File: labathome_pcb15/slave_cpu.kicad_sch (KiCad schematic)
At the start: 43 parts, among them J1 HALL, J26 STDC14, J27 ADDA, J28 Brushless, J31 Servo1, J32 Servo2, J33 Servo3, SW10 USBPD ADC2 EXT, U3 DRV8313, U5 STM32G431C6Ux, Y1 8MHz/12pF

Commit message: Final PCB as ordered @ JLCPCB
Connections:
- net STM32_RESET: now also J26.12 (Pin_12)
- no-connect marks 8 -> 7
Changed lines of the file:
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@@
-	)
-	(no_connect
-		(at 48.26 113.03)
 	)
 	(no_connect
@@
 			(effects
 				(font
+					(size 1.27 1.27)
+				)
+				(justify left)
+				(hide yes)
+			)
+		)
+	)
+	(global_label "STM32_RESET"
+		(shape output)
+		(at 48.26 113.03 0)
+		(fields_autoplaced yes)
+		(effects
+			(font
+				(size 1.27 1.27)
+			)
+			(justify left)
+		)
+		(property "Intersheetrefs" "${INTERSHEET_REFS}"
+			(at 64.0054 113.03 0)
+			(effects
+				(font

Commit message: lbathome 15.1
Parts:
- removed R65: 10k, Resistor_SMD:R_0402_1005Metric, symbol Device:R
- removed SW10: USBPD ADC2 EXT, liebler_MECH:SW_SPDT_PCM12_handsolder, symbol liebler_MECH:SW_SPDT_with_Case
- removed U5: STM32G431C6Ux, Package_DFN_QFN:QFN-48-1EP_7x7mm_P0.5mm_EP5.6x5.6mm, symbol MCU_ST_STM32G4:STM32G431C6Ux
- removed Y1: 8MHz/12pF, Crystal:Crystal_SMD_3225-4Pin_3.2x2.5mm, symbol Device:Crystal_GND24
- added C52, C63: u1/50V, Capacitor_SMD:C_0603_1608Metric, symbol Device:C
- added C64: u1, Capacitor_SMD:C_0603_1608Metric, symbol Device:C
- added J30: Servo4, liebler_CONN:PinHeader_1x03_P2.54mm_Vertical_smallerCourtyard, symbol Connector_Generic:Conn_01x03
- added J34: STM32 EXT, Connector_PinHeader_2.54mm:PinHeader_2x03_P2.54mm_Vertical, symbol Connector_Generic:Conn_02x03_Odd_Even
- added R38: r1, Resistor_THT:R_Axial_DIN0309_L9.0mm_D3.2mm_P12.70mm_Horizontal, symbol Device:R
- added U16: LM358, Package_SO:SOIC-8_3.9x4.9mm_P1.27mm, symbol Amplifier_Operational:LM358
- added U5: STM32G431R8Tx, Package_QFP:LQFP-64_10x10mm_P0.5mm, symbol MCU_ST_STM32G4:STM32G431R8Tx
- C50: value 15p -> u1
- C61: value 15p -> 4u7/6V3
- FB2: value 600R -> 600R
- J31, J32, J33: footprint Connector_PinHeader_2.54mm:PinHeader_1x03_P2.54mm_Vertical -> liebler_CONN:PinHeader_1x03_P2.54mm_Vertical_smallerCourtyard
- R49: value k22 -> 10k; footprint Resistor_SMD:R_0402_1005Metric -> Resistor_SMD:R_0805_2012Metric_Pad1.20x1.40mm_HandSolder
- R52: value 10k -> 22k; footprint Resistor_SMD:R_0402_1005Metric -> Resistor_SMD:R_0805_2012Metric_Pad1.20x1.40mm_HandSolder; Option (none) -> Sound only
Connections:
- net ADC_IN2_EXT is gone; now on net ADC_IN2: J27.4 (Pin_4)
- net +24V: now also C52.2, C63.1, C64.2, U16.8 (V+)
- net +3V3: now also C50.1, U5.1 (VBAT), U5.16 (VDD), U5.32 (VDD), U5.48 (VDD), U5.64 (VDD); no longer R50.2, R52.2, U3.15 (V3P3)
- net +5V: now also J30.2 (Pin_2)
- net ADC_IN1: now also U5.22 (PC4)
- net ADC_IN2: now also U5.23 (PC5)
- net BL_DRV1: now also U5.38 (PC6)
- net BL_DRV2: now also U5.39 (PC7)
- net BL_DRV3: now also U5.40 (PC8)
- net BL_ENABLEx: now also U5.60 (PB7)
- net BL_FAULT: now also U5.41 (PC9); no longer R50.1
- net BL_HALL1: now also U5.24 (PB0)
- net BL_HALL2: now also U5.21 (PA7)
- net BL_HALL3: now also U5.20 (PA6)
- net BL_RESET: now also U5.55 (PD2)
- net BL_SLEEP: now also U5.42 (PA8); no longer R52.1
- net BRIGHTNESS: now also U5.5 (PF0)
- net BTN_RED: now also U5.61 (PB8)
- net BTN_YEL: now also U5.6 (PF1)
- net DAC1_OUT1: now also U5.18 (PA4)
- net DAC1_OUT2: now also R50.2, U16.3 (+), U5.19 (PA5); no longer J27.2 (Pin_2)
- net FAN2_DRIVE: now also U5.14 (PA2)
- net GND: now also C50.2, C61.2, R49.1, R50.1, C52.1, C63.2, C64.1, J30.3 (Pin_3), R38.2, U16.4 (V-), U5.15 (VSS), U5.27 (VSSA), U5.31 (VSS), U5.47 (VSS), U5.63 (VSS); no longer C50.1, C61.1, U3.10 (PGND3), U3.6 (PGND1), U3.7 (PGND2)
- net HEATER: now also U5.3 (PC14)
- net LED_INFO: now also U5.54 (PC12)
- net LED_WHITE_P: now also U5.17 (PA3)
- net MOVE: now also U5.2 (PC13)
- net ROT_A: now also U5.12 (PA0)
- net ROT_B: now also U5.13 (PA1)
- net Relais: now also U5.4 (PC15)
- net SCL: now also U5.51 (PA15)
- net SDA: now also U5.62 (PB9)
- net STM32_RESET: now also U5.7 (PG10)
- net SWCLK: now also U5.50 (PA14)
- net SWDIO: now also U5.49 (PA13)
- net Servo1: now also U5.8 (PC0)
- net Servo2: now also U5.9 (PC1)
- net Servo3: now also U5.10 (PC2)
- net UART4_RX: now also U5.53 (PC11)
- net UART4_TX: now also U5.52 (PC10)
- net USBPD_CC1: now also U5.43 (PA9), U5.59 (PB6)
- net USBPD_CC2: now also U5.44 (PA10), U5.57 (PB4)
- net USBPD_D+: now also U5.46 (PA12)
- net USBPD_D-: now also U5.45 (PA11)
- net at R49.2: now also R52.2, U16.2 (-); no longer C50.2
- net 24V_SENSE: now reaches R68.2, R69.1
- net 24V_SENSE: now also U5.37 (PB15)
- net at C37.1, C49.1, FB2.1: now also U5.28 (VREF+), U5.29 (VDDA)
- new net: R52.1, U16.1, U16.5 (+)
- new net: C61.1, U3.15 (V3P3)
- new net BL_ISENSE: R38.1, U3.10 (PGND3), U3.6 (PGND1), U3.7 (PGND2), U5.36 (PB14)
- new net DAC1_OUT2x: J27.2 (Pin_2), U16.6 (-), U16.7
- new net OPAMP3+: J34.2 (Pin_2), U5.35 (PB13)
- new net OPAMP3-: J34.3 (Pin_3), U5.26 (PB2)
- new net OPAMP3Q: J34.5 (Pin_5), U5.25 (PB1)
- new net PB12: J34.4 (Pin_4), U5.34 (PB12)
- new net Servo4: J30.1 (Pin_1), U5.11 (PC3)
- new net UART3_RX: J34.1 (Pin_1), U5.33 (PB11)
- new net UART3_TX: J34.6 (Pin_6), U5.30 (PB10)
- no-connect marks 7 -> 5
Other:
- note added: "ADC1.12"
- note added: "BL_DRV=TIM8 Encoder=TIM2 BL_HALL=TIM3 Servos=TIM1 White LED + FAN=TIM15"
- note added: "BOOT0!"
- note added: "I2C1.C"
- note added: "I2C3.C"
- note added: "OPAMP2.+"
- note added: "OPAMP3.+"
- note added: "OPAMP3.-"
- note added: "OPAMP3.OUT"
- note added: "Overcurrent ca. 1,5A"
- note added: "T15.1"
- note added: "T15.2"
- note added: "T17.1N"
- note added: "U2.T"
- note added: "U3.R"
- note added: "U3.T"
- note removed: "ADC1.11"
- note removed: "ADC12.14"
- note removed: "Annahme Streukapaität 5pF Lastkapazität = (12pF-5pF)*2=15pF"
- note removed: "I2C1.D T4.2 T3.4"
- note removed: "Input"
- note removed: "PB13"
- note removed: "PIR?"
- note removed: "Slow Software-PWM!"
- note removed: "T1.1 I2C2.D"
- note removed: "T1.2 I2C2.C T2.3 CC1"
- note removed: "T1.3 T2.4 CC2"
- note removed: "T16.1 T3.1 ADC2.3"
- note removed: "T16.1 T4.3 T8.2 Boot0"
- note removed: "T17.1 T3.2 ADC2.4"
- note removed: "T2.1 ADC12.1"
- note removed: "T2.1 T8.1 I2C1.C"
- note removed: "T2.2"
- note removed: "T2.2 ADC12.2"
- note removed: "T2.3"
- note removed: "T2.3 T15.1"
- note removed: "T2.4 T15.2"
- note removed: "T3.1 T8.1"
- note removed: "T3.2 I2C3.D"
- note removed: "T3.3 ADC1.15"
- note removed: "T3.4 ADC1.12"
- note removed: "T4.4"
- moved on the sheet: C25, C39, D19, FB2, R34

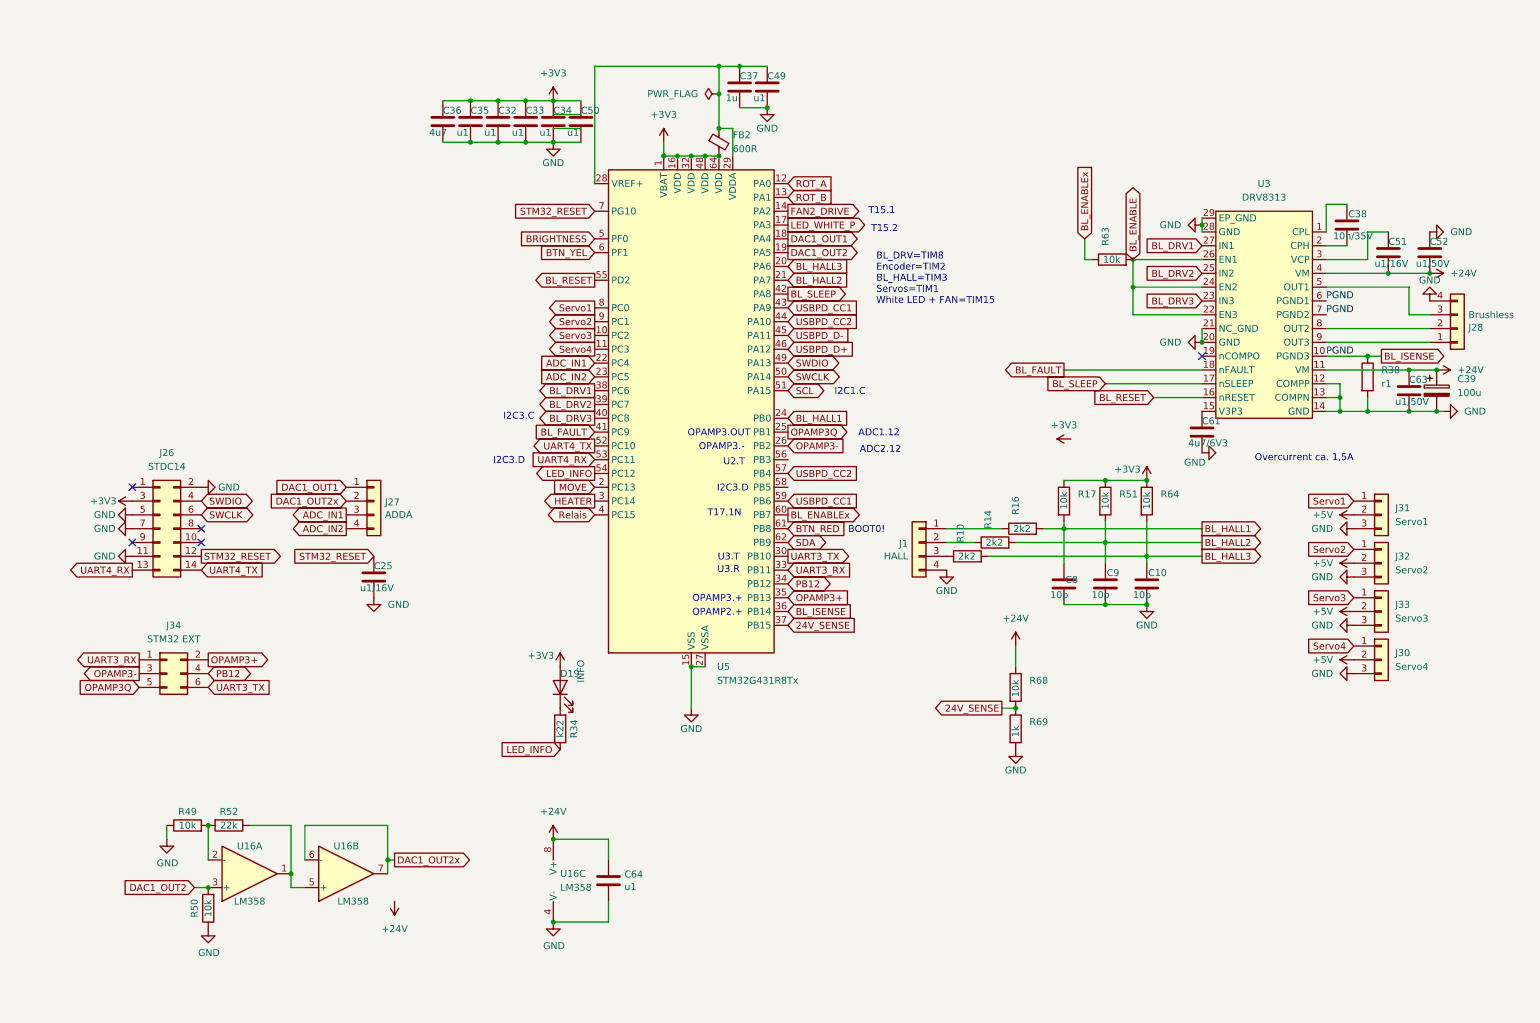
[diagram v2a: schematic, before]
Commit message: Updates in PCB, arduino test firmware
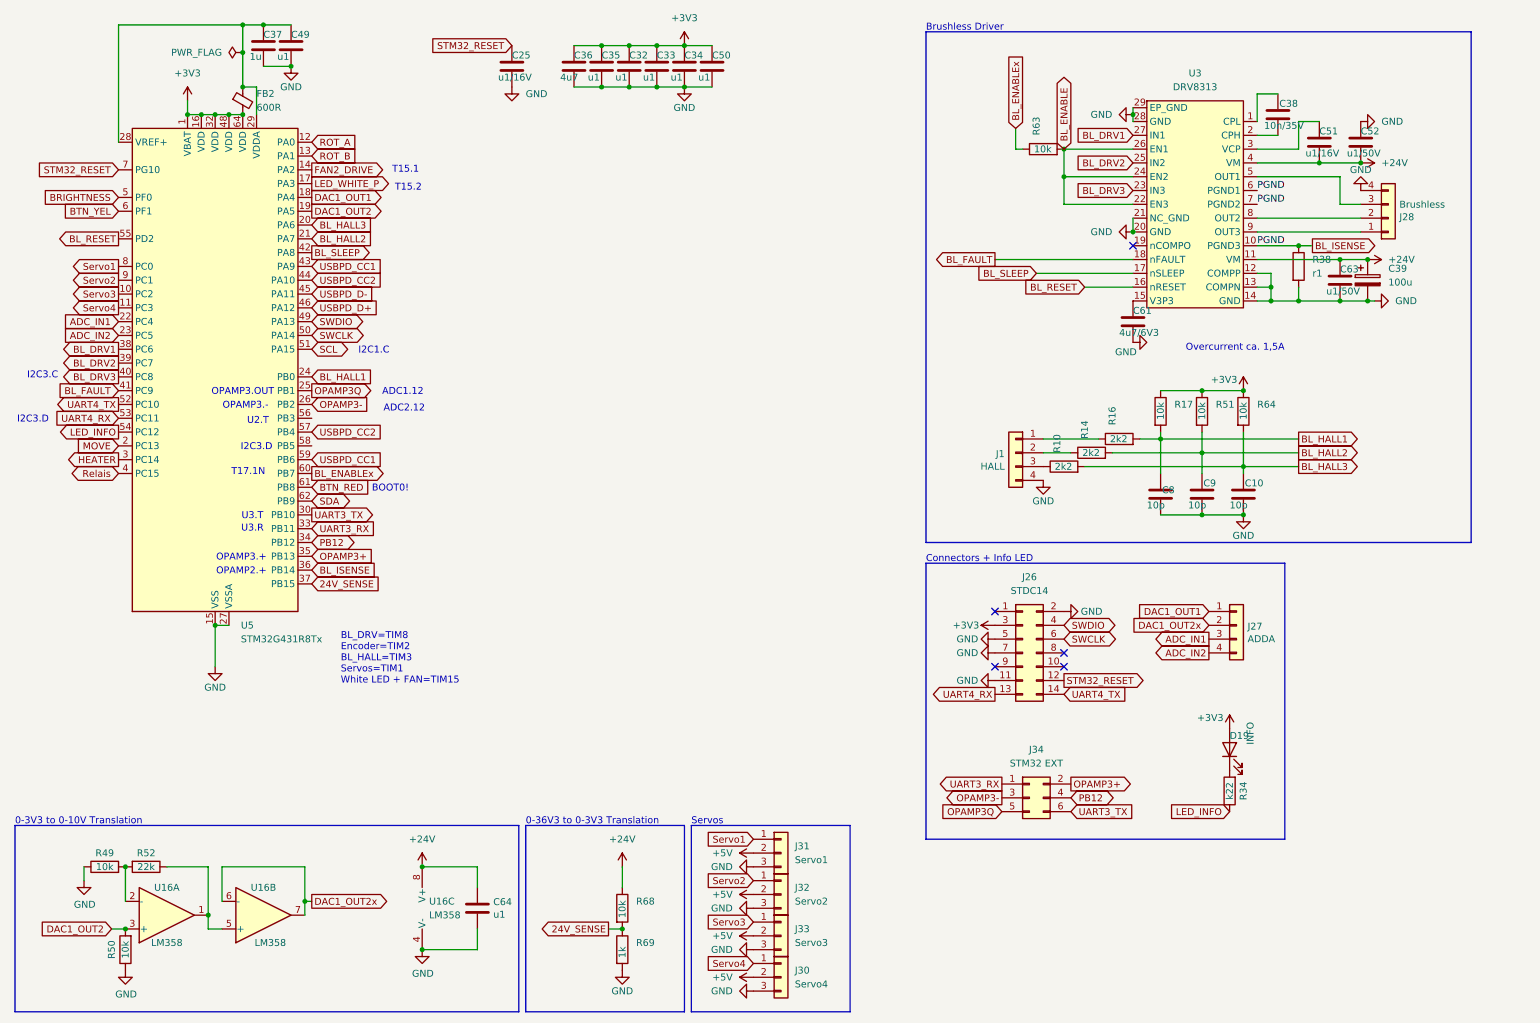
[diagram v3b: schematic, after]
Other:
- note added: "0-36V3 to 0-3V3 Translation"
- note added: "0-3V3 to 0-10V Translation"
- note added: "Brushless Driver"
- note added: "Connectors + Info LED"
- note added: "Servos"
- company: (none) -> Klaus Liebler
- title: (none) -> lab@home
- moved on the sheet: C10, C25, C32, C33, C34, C35, C36, C37, C38, C39, C49, C50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

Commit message: Re-enumerate Servos and Fans
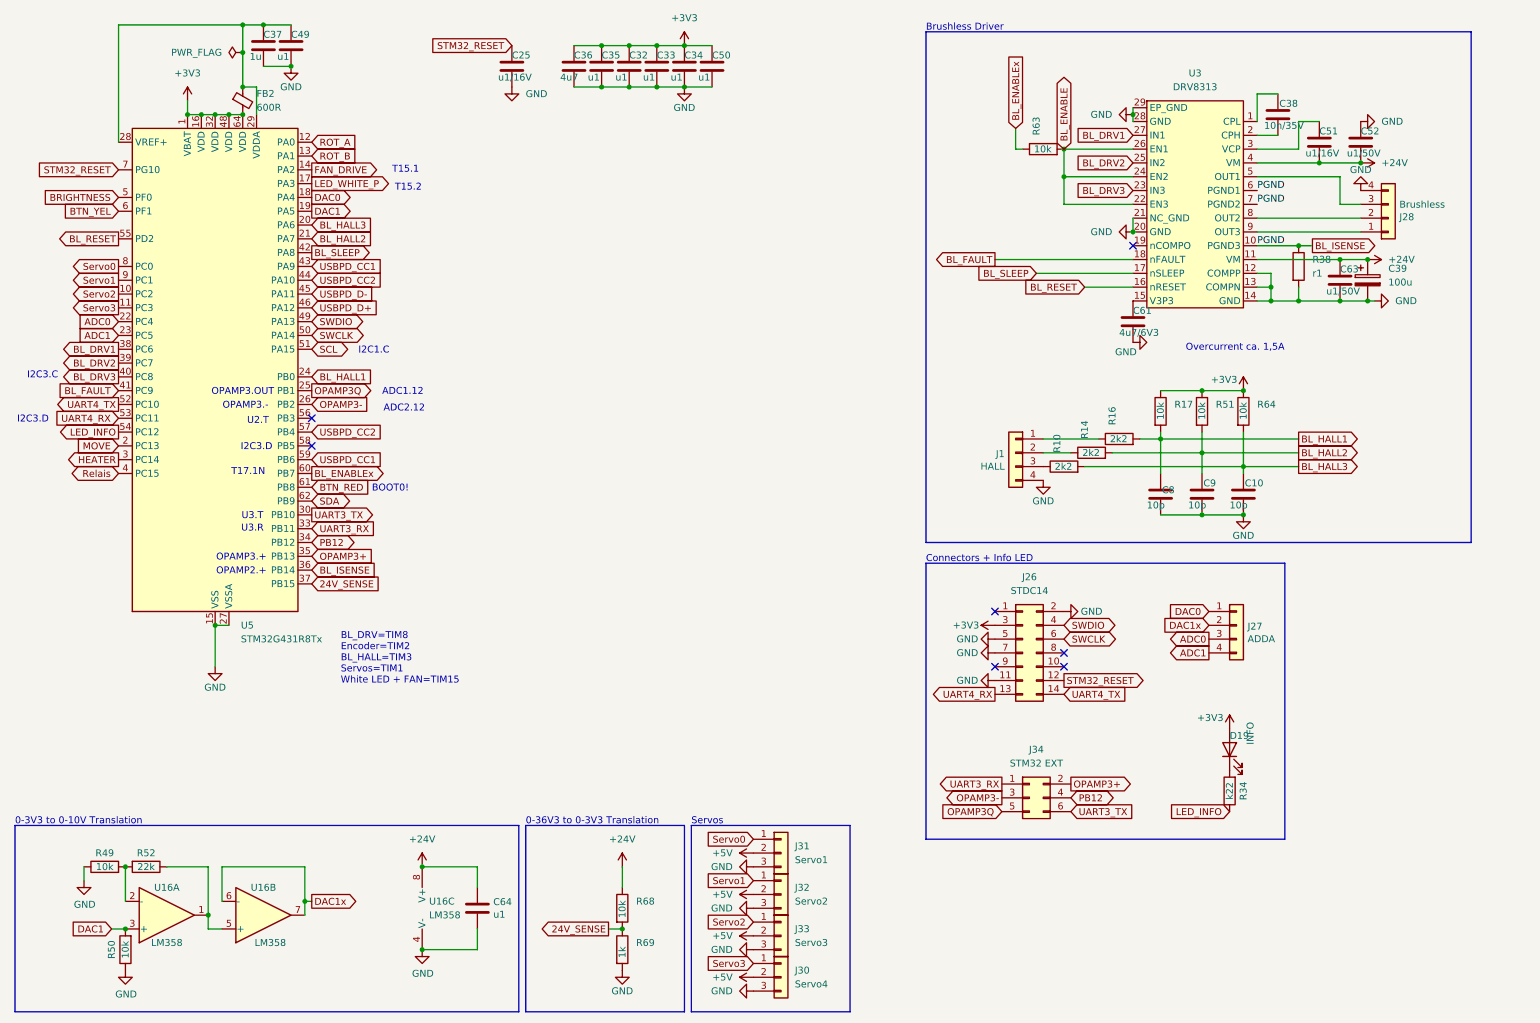
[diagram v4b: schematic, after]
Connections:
- net Servo4 is gone; now on net Servo3: J30.1 (Pin_1), U5.11 (PC3)
- net Servo1: now also J32.1 (Pin_1), U5.9 (PC1); no longer J31.1 (Pin_1), U5.8 (PC0)
- net Servo2: now also J33.1 (Pin_1), U5.10 (PC2); no longer J32.1 (Pin_1), U5.9 (PC1)
- net Servo3: no longer J33.1 (Pin_1), U5.10 (PC2)
- net ADC_IN1 renamed ADC0
- net ADC_IN2 renamed ADC1
- net DAC1_OUT1 renamed DAC0
- net DAC1_OUT2 renamed DAC1
- net DAC1_OUT2x renamed DAC1x
- net FAN2_DRIVE renamed FAN_DRIVE
- new net Servo0: J31.1 (Pin_1), U5.8 (PC0)
- no-connect marks 5 -> 7
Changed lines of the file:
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@@
 	)
 	(no_connect
+		(at 68.58 87.63)
+	)
+	(no_connect
 		(at 219.71 55.88)
 	)
@@
 		(at 207.01 133.35)
 	)
+	(no_connect
+		(at 68.58 92.71)
+	)
 	(wire
 		(pts
@@
 		)
 	)
-	(global_label "Servo1"
+	(global_label "Servo0"
 		(shape output)
 		(at 33.02 59.69 180)
@@
 		)
 	)
-	(global_label "Servo4"
+	(global_label "Servo3"
 		(shape input)
 		(at 149.86 187.96 180)
@@
 		)
 	)
-	(global_label "DAC1_OUT2x"
+	(global_label "DAC1x"
 		(shape output)
 		(at 68.58 176.53 0)
@@
 		)
 		(property "Intersheetrefs" "${INTERSHEET_REFS}"
-			(at 83.2371 176.53 0)
+			(at 77.4314 176.53 0)
 			(effects
 				(font
@@
 		)
 	)
-	(global_label "Servo4"
+	(global_label "Servo3"
 		(shape output)
 		(at 33.02 67.31 180)
@@
 		)
 	)
-	(global_label "DAC1_OUT2"
+	(global_label "DAC1"
 		(shape output)
 		(at 68.58 49.53 0)
@@
 		)
 		(property "Intersheetrefs" "${INTERSHEET_REFS}"
-			(at 82.209 49.53 0)
+			(at 76.4033 49.53 0)
 			(effects
 				(font
@@
 		)
 	)
-	(global_label "Servo2"
+	(global_label "Servo1"
 		(shape output)
 		(at 33.02 62.23 180)
@@
 		)
 	)
-	(global_label "ADC_IN2"
+	(global_label "ADC1"
 		(shape input)
 		(at 33.02 72.39 180)
@@
 		)
 		(property "Intersheetrefs" "${INTERSHEET_REFS}"
-			(at 22.2938 72.39 0)
+			(at 25.1967 72.39 0)
 			(effects
 				(font
@@
 		)
 	)
-	(global_label "Servo2"
+	(global_label "Servo1"
 		(shape input)
 		(at 149.86 172.72 180)
@@
 		)
 	)
-	(global_label "ADC_IN1"
+	(global_label "ADC0"
 		(shape input)
 		(at 33.02 69.85 180)
@@
 		)
 		(property "Intersheetrefs" "${INTERSHEET_REFS}"
-			(at 22.2938 69.85 0)
+			(at 25.1967 69.85 0)
 			(effects
 				(font
@@
 		)
 	)
-	(global_label "Servo1"
+	(global_label "Servo0"
 		(shape input)
 		(at 149.86 165.1 180)
@@
 		)
 	)
-	(global_label "DAC1_OUT2x"
+	(global_label "DAC1x"
 		(shape input)
 		(at 233.68 125.73 180)
@@
 		)
 		(property "Intersheetrefs" "${INTERSHEET_REFS}"
-			(at 219.0229 125.73 0)
+			(at 224.8286 125.73 0)
 			(effects
 				(font
@@
 		)
 	)
-	(global_label "DAC1_OUT1"
+	(global_label "DAC0"
 		(shape output)
 		(at 68.58 46.99 0)
@@
 		)
 		(property "Intersheetrefs" "${INTERSHEET_REFS}"
-			(at 82.209 46.99 0)
+			(at 76.4033 46.99 0)
 			(effects
 				(font
@@
 		)
 	)
-	(global_label "ADC_IN1"
+	(global_label "ADC0"
 		(shape output)
 		(at 233.68 128.27 180)
@@
 		)
 		(property "Intersheetrefs" "${INTERSHEET_REFS}"
-			(at 222.9538 128.27 0)
+			(at 225.8567 128.27 0)
 			(effects
 				(font
@@
 		)
 	)
-	(global_label "Servo3"
+	(global_label "Servo2"
 		(shape output)
 		(at 33.02 64.77 180)
@@
 		)
 	)
-	(global_label "FAN2_DRIVE"
+	(global_label "FAN_DRIVE"
 		(shape output)
 		(at 68.58 41.91 0)
@@
 		)
 		(property "Intersheetrefs" "${INTERSHEET_REFS}"
-			(at 82.6324 41.91 0)
+			(at 81.4229 41.91 0)
 			(effects
 				(font
@@
 		)
 	)
-	(global_label "DAC1_OUT2"
+	(global_label "DAC1"
 		(shape input)
 		(at 31.75 181.61 180)
@@
 		)
 		(property "Intersheetrefs" "${INTERSHEET_REFS}"
-			(at 18.121 181.61 0)
+			(at 23.9267 181.61 0)
 			(effects
 				(font
@@
 		)
 	)
-	(global_label "Servo3"
+	(global_label "Servo2"
 		(shape input)
 		(at 149.86 180.34 180)
@@
 		)
 	)
-	(global_label "ADC_IN2"
+	(global_label "ADC1"
 		(shape output)
 		(at 233.68 130.81 180)
@@
 		)
 		(property "Intersheetrefs" "${INTERSHEET_REFS}"
-			(at 222.9538 130.81 0)
+			(at 225.8567 130.81 0)
 			(effects
 				(font
@@
 		)
 	)
-	(global_label "DAC1_OUT1"
+	(global_label "DAC0"
 		(shape input)
 		(at 233.68 123.19 180)
@@
 		)
 		(property "Intersheetrefs" "${INTERSHEET_REFS}"
-			(at 220.051 123.19 0)
+			(at 225.8567 123.19 0)
 			(effects
 				(font
